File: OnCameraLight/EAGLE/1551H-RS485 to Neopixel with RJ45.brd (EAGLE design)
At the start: 54 x 29 mm, 8 parts, among them IC1 75176AP, J1 RJHSE-5381

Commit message: Go through and fix notation on RS485 wiring everywhere to use the standard A/B notation.
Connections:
- net DATA2+ renamed DATA2B
- net DATA2- renamed DATA2A
- net RS485+ renamed RS485B
- net RS485- renamed RS485A
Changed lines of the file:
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@@
 <setting verticaltext="up"/>
 </settings>
-<grid distance="15" unitdist="mil" unit="mil" style="lines" multiple="1" display="no" altdistance="5" altunitdist="mil" altunit="mil"/>
+<grid distance="5" unitdist="mil" unit="mil" style="lines" multiple="1" display="no" altdistance="5" altunitdist="mil" altunit="mil"/>
 <layers>
 <layer number="1" name="Top" color="4" fill="1" visible="yes" active="yes"/>
@@
 <board>
 <plain>
-<wire x1="24.51" y1="18.13" x2="46.1" y2="18.13" width="0.1524" layer="25"/>
 <text x="43.18" y="20.32" size="1.778" layer="26" rot="MR0">Fits Hammond
 1551H</text>
@@
 <text x="16.764" y="14.859" size="1.016" layer="25">RS485 Neopixel
 Driver Over Ethernet</text>
+<wire x1="24.638" y1="28.194" x2="46.101" y2="28.194" width="0.1524" layer="25"/>
+<wire x1="46.101" y1="28.194" x2="46.101" y2="18.161" width="0.1524" layer="25"/>
+<wire x1="46.101" y1="18.161" x2="24.892" y2="18.161" width="0.1524" layer="25"/>
 </plain>
 <attributes>
@@
 <wire x1="12.7" y1="26.67" x2="18.66" y2="20.71" width="0.508" layer="1"/>
 </signal>
-<signal name="RS485+">
-<contactref element="R1" pad="1"/>
-<contactref element="IC1" pad="7"/>
-<contactref element="J1" pad="1"/>
-<wire x1="21.74" y1="5.08" x2="25.55" y2="8.89" width="0.3048" layer="1"/>
-<wire x1="29.86" y1="6.97" x2="29.86" y2="2.19" width="0.3048" layer="1"/>
-<wire x1="25.55" y1="8.89" x2="27.94" y2="8.89" width="0.3048" layer="1"/>
-<wire x1="27.94" y1="8.89" x2="29.86" y2="6.97" width="0.3048" layer="1"/>
-<wire x1="29.86" y1="2.19" x2="34.02" y2="6.35" width="0.3048" layer="1"/>
-<wire x1="34.02" y1="6.35" x2="36.83" y2="6.35" width="0.3048" layer="1"/>
-<wire x1="36.83" y1="6.35" x2="38.31" y2="7.83" width="0.3048" layer="1"/>
-<wire x1="38.31" y1="7.83" x2="38.31" y2="8.62" width="0.3048" layer="1"/>
-</signal>
-<signal name="RS485-">
-<contactref element="R1" pad="2"/>
-<contactref element="IC1" pad="6"/>
-<contactref element="J1" pad="2"/>
-<wire x1="20.72" y1="6.86" x2="22.1" y2="6.86" width="0.3048" layer="1"/>
-<wire x1="27.59" y1="12.35" x2="29.86" y2="12.35" width="0.3048" layer="1"/>
-<wire x1="22.1" y1="6.86" x2="27.59" y2="12.35" width="0.3048" layer="1"/>
-<wire x1="29.86" y1="12.35" x2="33.37" y2="12.35" width="0.3048" layer="1"/>
-<wire x1="35.77" y1="9.95" x2="35.77" y2="8.62" width="0.3048" layer="1"/>
-<wire x1="33.37" y1="12.35" x2="35.77" y2="9.95" width="0.3048" layer="1"/>
-</signal>
 <signal name="NEODATA">
 <contactref element="R2" pad="1"/>
@@
 <wire x1="40.85" y1="17.57" x2="39.37" y2="19.05" width="0.3048" layer="16"/>
 </signal>
-<signal name="DATA2+">
+<signal name="DATA2B">
 <contactref element="J1" pad="3"/>
 </signal>
-<signal name="DATA2-">
+<signal name="DATA2A">
 <contactref element="J1" pad="6"/>
 </signal>
@@
 <wire x1="4.56" y1="17.26" x2="7.62" y2="20.32" width="0.3048" layer="16"/>
 </signal>
+<signal name="RS485B">
+<contactref element="J1" pad="1"/>
+<contactref element="IC1" pad="7"/>
+<contactref element="R1" pad="1"/>
+<wire x1="29.86" y1="6.97" x2="29.86" y2="2.19" width="0.3048" layer="1"/>
+<wire x1="25.55" y1="8.89" x2="27.94" y2="8.89" width="0.3048" layer="1"/>
+<wire x1="27.94" y1="8.89" x2="29.86" y2="6.97" width="0.3048" layer="1"/>
+<wire x1="29.86" y1="2.19" x2="34.02" y2="6.35" width="0.3048" layer="1"/>
+<wire x1="34.02" y1="6.35" x2="36.83" y2="6.35" width="0.3048" layer="1"/>
+<wire x1="36.83" y1="6.35" x2="38.2905" y2="7.8105" width="0.3048" layer="1"/>
+<wire x1="21.74" y1="5.08" x2="25.55" y2="8.89" width="0.3048" layer="1"/>
+<wire x1="38.31" y1="8.62" x2="38.31" y2="7.83" width="0.3048" layer="1"/>
+<wire x1="38.31" y1="7.83" x2="38.2905" y2="7.8105" width="0.3048" layer="1"/>
+</signal>
+<signal name="RS485A">
+<contactref element="J1" pad="2"/>
+<contactref element="IC1" pad="6"/>
+<contactref element="R1" pad="2"/>
+<wire x1="27.59" y1="12.35" x2="29.86" y2="12.35" width="0.3048" layer="1"/>
+<wire x1="22.1" y1="6.86" x2="27.59" y2="12.35" width="0.3048" layer="1"/>
+<wire x1="29.86" y1="12.35" x2="33.37" y2="12.35" width="0.3048" layer="1"/>
+<wire x1="35.77" y1="9.95" x2="33.37" y2="12.35" width="0.3048" layer="1"/>
+<wire x1="35.77" y1="8.62" x2="35.77" y2="9.95" width="0.3048" layer="1"/>
+<wire x1="20.72" y1="6.86" x2="22.1" y2="6.86" width="0.3048" layer="1"/>
+</signal>
 </signals>

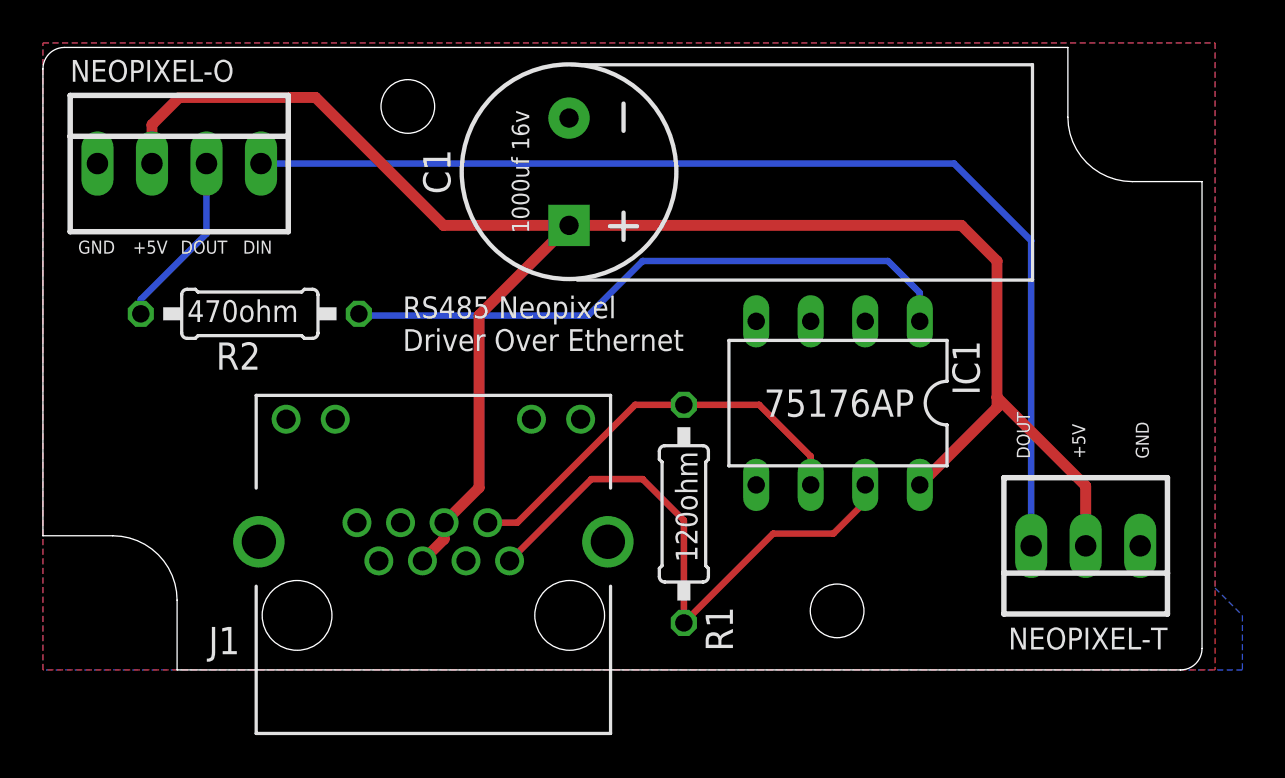
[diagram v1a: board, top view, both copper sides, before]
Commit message: Revisions to boards after working with initial prototypes.
- Update boards to use SMD components to help save on space.
- Redesign wireless receiver to use 3.3v logic to avoid using the Xbee breakout.
- Remove designs that aren't going to be used.
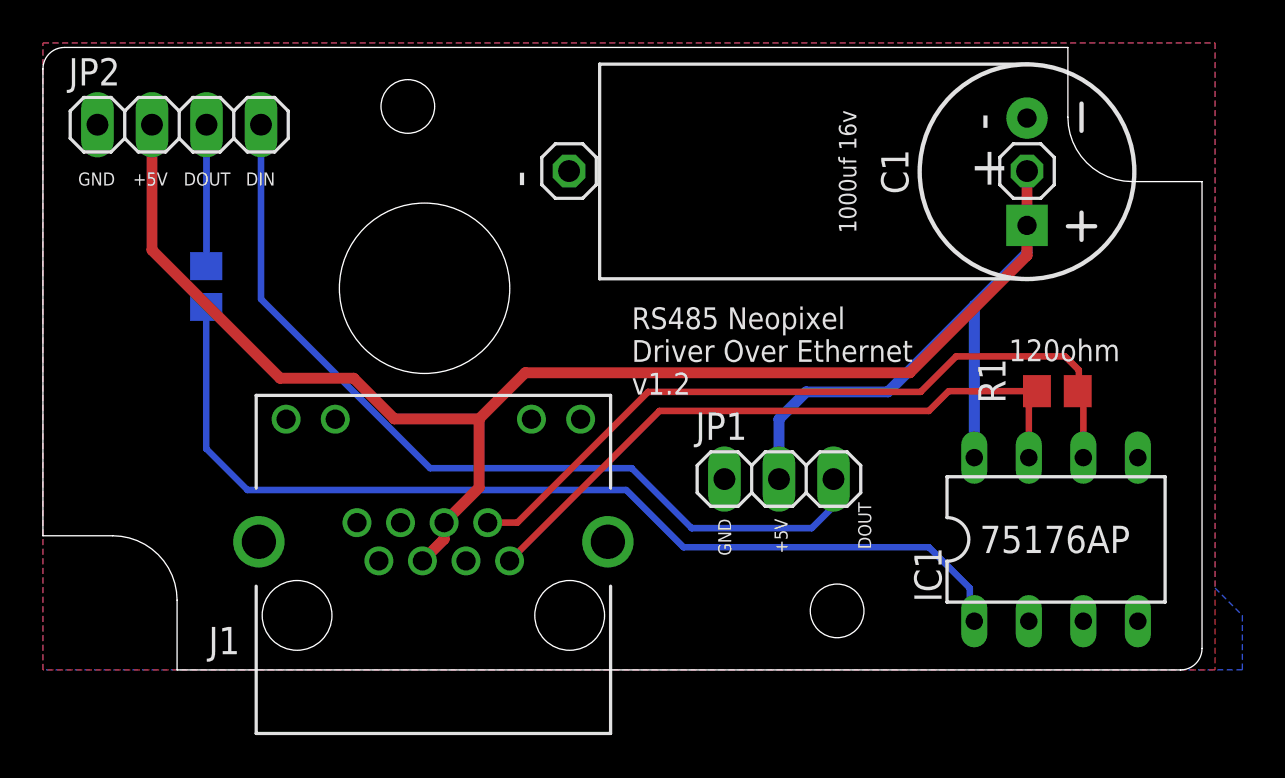
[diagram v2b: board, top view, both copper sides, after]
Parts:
- removed NEOPIXEL-O: 22-23-2041, con-molex:22-23-2041
- removed NEOPIXEL-T: 22-23-2031, con-molex:22-23-2031
- added JP1: NEOPIXEL-T, pinhead:1X03
- added JP2: NEOPIXEL-O, pinhead:1X04
- added JP3, JP4: (no value), pinhead:1X01
- R1, R2: device rcl:0207/10 -> rcl:R0805
- moved C1 21.3 mm to (45.8, 23.2)
- moved R1 18.3 mm to (47.3, 13.0), turned to 0 degrees
- moved IC1 12.0 mm to (47.2, 6.08), turned to 0 degrees
- moved R2 2.40 mm to (7.61, 17.9), flipped to the bottom, turned to 90 degrees
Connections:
- net GND: now also JP1.1, JP2.1, JP3.1; no longer NEOPIXEL-O.1, NEOPIXEL-T.1
- net NEO-O: now also JP2.3; no longer NEOPIXEL-O.3
- net NEO-T: now also JP1.3, JP2.4; no longer NEOPIXEL-O.4, NEOPIXEL-T.3
- net VCC: now also JP1.2, JP2.2, JP4.1; no longer NEOPIXEL-O.2, NEOPIXEL-T.2
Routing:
- net NEODATA: track 29.2 -> 46.5 mm
- net RS485A: track 19.6 -> 35.2 mm
- net NEO-T: track 51.6 -> 40.9 mm
- net VCC: track 83.9 -> 90.6 mm
- net RS485B: track 26.8 -> 31.1 mm
- net NEO-O: track 8.27 -> 6.59 mm
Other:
- board text added: "+"
- board text added: "-"
- board text added: "RS485 Neopixel Driver Over Ethernet v1.2"
- board text removed: "RS485 Neopixel Driver Over Ethernet"

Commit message: Add decoupling caps
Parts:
- added C2: (no value), Nordic_nRF:RESC0805_N
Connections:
- net GND: now also C2.2
- net VCC: now also C2.1
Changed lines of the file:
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@@
 <layer number="115" name="ReferenceISLANDS" color="7" fill="1" visible="yes" active="yes"/>
 <layer number="116" name="Patch_BOT" color="9" fill="4" visible="yes" active="yes"/>
+<layer number="117" name="BACKMAAT1" color="7" fill="1" visible="yes" active="yes"/>
 <layer number="118" name="Rect_Pads" color="7" fill="1" visible="yes" active="yes"/>
+<layer number="119" name="KAP_TEKEN" color="7" fill="1" visible="yes" active="yes"/>
+<layer number="120" name="KAP_MAAT1" color="7" fill="1" visible="yes" active="yes"/>
 <layer number="121" name="_tsilk" color="7" fill="1" visible="yes" active="yes"/>
 <layer number="122" name="_bsilk" color="7" fill="1" visible="yes" active="yes"/>
@@
 <layer number="128" name="_bValues" color="7" fill="1" visible="yes" active="yes"/>
 <layer number="129" name="Mask" color="7" fill="1" visible="yes" active="yes"/>
+<layer number="130" name="SMDSTROOK" color="7" fill="1" visible="yes" active="yes"/>
 <layer number="131" name="tAdjust" color="7" fill="1" visible="yes" active="yes"/>
 <layer number="132" name="bAdjust" color="7" fill="1" visible="yes" active="yes"/>
+<layer number="133" name="bottom_silk" color="7" fill="1" visible="yes" active="yes"/>
 <layer number="144" name="Drill_legend" color="7" fill="1" visible="yes" active="yes"/>
 <layer number="150" name="Notes" color="7" fill="1" visible="yes" active="yes"/>
@@
 <attribute name="VALUE" x="44.577" y="20.066" size="1.27" layer="27"/>
 </element>
+<element name="C2" library="Nordic_nRF" library_urn="urn:adsk.eagle:library:169009" package="RESC0805_N" package3d_urn="urn:adsk.eagle:package:2593736/1" value="" x="42.164" y="12.192" smashed="yes" rot="MR0">
+<attribute name="NAME" x="43.164" y="13.692" size="1.27" layer="26" rot="MR0"/>
+<attribute name="VALUE" x="43.164" y="9.692" size="1.27" layer="28" rot="MR0"/>
+</element>
 </elements>
 <signals>
@@
 <contactref element="JP1" pad="1"/>
 <contactref element="JP3" pad="1"/>
+<contactref element="C2" pad="2"/>
 </signal>
 <signal name="VCC">
@@
 <wire x1="45.847" y1="23.241" x2="45.847" y2="20.711" width="0.508" layer="1"/>
 <wire x1="45.847" y1="20.711" x2="45.846" y2="20.71" width="0.508" layer="1"/>
-<wire x1="43.39" y1="9.89" x2="43.39" y2="16.974" width="0.508" layer="16"/>
 <wire x1="45.846" y1="19.43" x2="45.846" y2="20.71" width="0.508" layer="16"/>
-<wire x1="45.846" y1="19.43" x2="43.39" y2="16.974" width="0.508" layer="16"/>
-<wire x1="43.39" y1="16.974" x2="39.37" y2="12.954" width="0.508" layer="16"/>
+<wire x1="45.846" y1="19.43" x2="43.434" y2="17.018" width="0.508" layer="16"/>
+<wire x1="43.264" y1="16.848" x2="39.37" y2="12.954" width="0.508" layer="16"/>
 <wire x1="35.56" y1="12.954" x2="34.29" y2="11.684" width="0.508" layer="16"/>
 <wire x1="34.29" y1="11.684" x2="34.29" y2="8.89" width="0.508" layer="16"/>
 <wire x1="39.37" y1="12.954" x2="35.56" y2="12.954" width="0.508" layer="16"/>
 <wire x1="5.08" y1="25.4" x2="5.08" y2="19.558" width="0.508" layer="1"/>
+<contactref element="C2" pad="1"/>
+<wire x1="43.39" y1="9.89" x2="43.39" y2="12.066" width="0.508" layer="16"/>
+<wire x1="43.39" y1="12.066" x2="43.264" y2="12.192" width="0.508" layer="16"/>
+<wire x1="43.264" y1="12.192" x2="43.264" y2="16.848" width="0.508" layer="16"/>
+<wire x1="43.264" y1="16.848" x2="43.434" y2="17.018" width="0.508" layer="16"/>
 </signal>
 <signal name="NEODATA">
